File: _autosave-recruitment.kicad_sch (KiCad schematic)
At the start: 0 parts

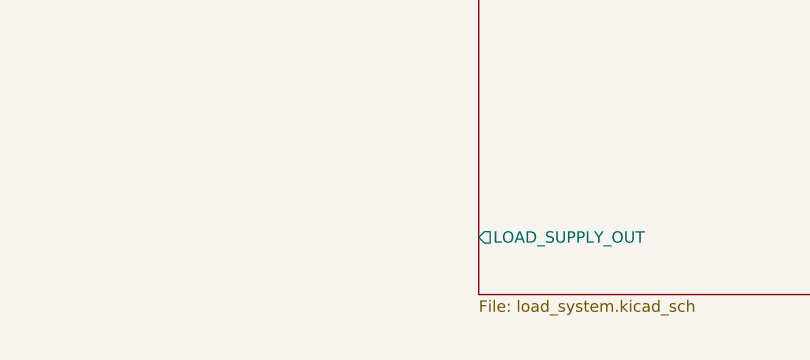
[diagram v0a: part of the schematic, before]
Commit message: feat:added resistor as a load and added demo connections to minimize ERC errors(2)
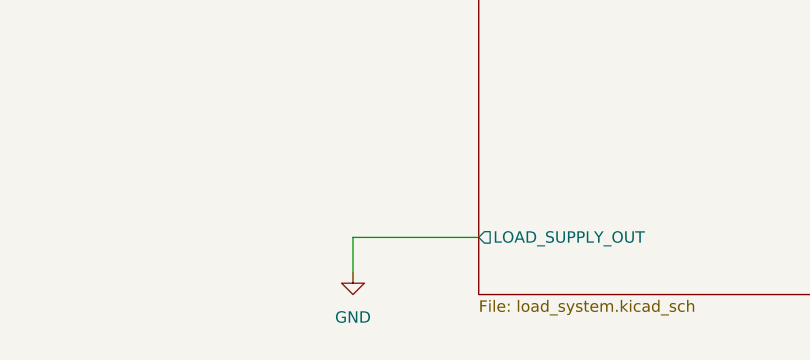
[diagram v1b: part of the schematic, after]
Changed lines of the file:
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@@
+	(wire
+		(pts
+			(xy 212.09 148.59) (xy 212.09 144.78)
+		)
+		(stroke
+			(width 0)
+			(type default)
+		)
+	)
 	(wire
 		(pts
 			(xy 157.48 68.58) (xy 226.06 68.58)
+		)
+		(stroke
+			(width 0)
+			(type default)
+		)
+	)
+	(wire
+		(pts
+			(xy 212.09 144.78) (xy 226.06 144.78)
 		)
 		(stroke
@@
 		)
 	)
+	(symbol
+		(lib_id "power:GND")
+		(at 212.09 148.59 0)
+		(unit 1)
+		(exclude_from_sim no)
+		(in_bom yes)
+		(on_board yes)
+		(dnp no)
+		(fields_autoplaced yes)
+		(property "Reference" "#PWR03"
+			(at 212.09 154.94 0)
+			(effects
+				(font
+					(size 1.27 1.27)
+				)
+				(hide yes)
+			)
+		)
+		(property "Value" "GND"
+			(at 212.09 153.67 0)
+			(effects
+				(font
+					(size 1.27 1.27)
+				)
+			)
+		)
+		(property "Footprint" ""
+			(at 212.09 148.59 0)
+			(effects
+				(font
+					(size 1.27 1.27)
+				)
+				(hide yes)
+			)
+		)
+		(property "Datasheet" ""
+			(at 212.09 148.59 0)
+			(effects
+				(font
+					(size 1.27 1.27)
+				)
+				(hide yes)
+			)
+		)
+		(property "Description" "Power symbol creates a global label with name \"GND\" , ground"
+			(at 212.09 148.59 0)
+			(effects
+				(font
+					(size 1.27 1.27)
+				)
+				(hide yes)
+			)
+		)
+		(pin "1"
+		)
+		(instances
+			(project "recruitment"
+				(path "/bdc7face-9f7c-4701-80bb-4cc144448db1"
+					(reference "#PWR03")
+					(unit 1)
+				)
+			)
+		)
+	)
